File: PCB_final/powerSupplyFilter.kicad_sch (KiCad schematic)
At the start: 3 parts, among them U10 MCP6001T-I_OT

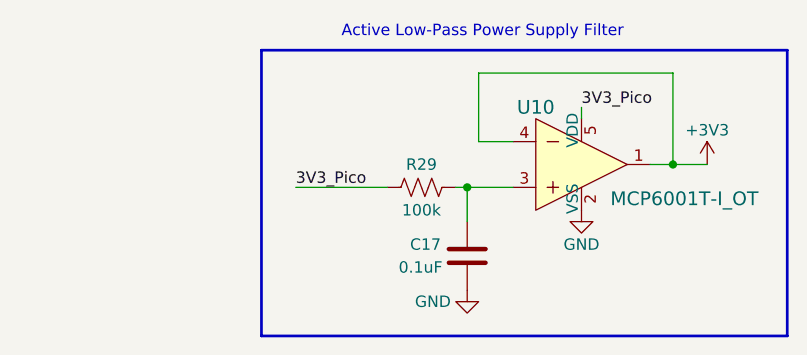
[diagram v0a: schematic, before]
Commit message: Removed filter from schematic and PCB. Adjusted tracings on PCB and schematic for ADC inputs so that each ADC has 14 inputs
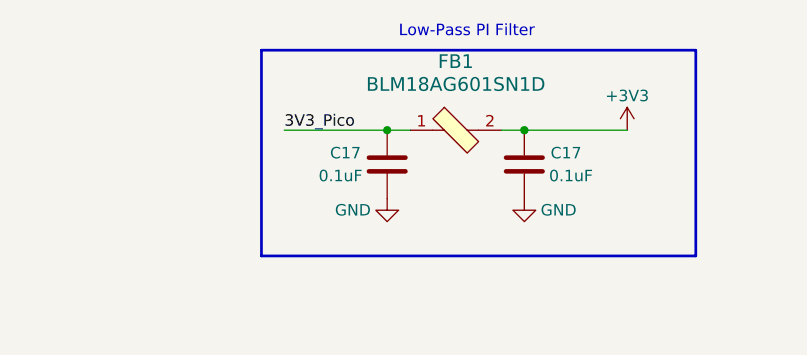
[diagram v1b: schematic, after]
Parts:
- removed R29: 100k, Resistor_SMD:R_0603_1608Metric, symbol Device:R_US
- removed U10: MCP6001T-I_OT, digikey-footprints:SOT-753, symbol dk_Linear-Amplifiers-Instrumentation-OP-Amps-Buffer-Amps:MCP6001T-I_OT
- added C17: 0.1uF, Capacitor_SMD:C_0603_1608Metric, symbol Device:C
- added FB1: BLM18AG601SN1D, digikey-footprints:0603, symbol dk_Ferrite-Beads-and-Chips:BLM18AG601SN1D
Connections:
- net +3V3: now also C17.1, FB1.2
- net 3V3_Pico: now also C17.1, FB1.1
- net GND: now also C17.2
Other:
- note added: "Low-Pass PI Filter"
- note removed: "Active Low-Pass Power Supply Filter"
- moved on the sheet: C17

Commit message: Updated filter's ferrite bead and capacitors on schematic and PCB. Power supply filter now fully integrated
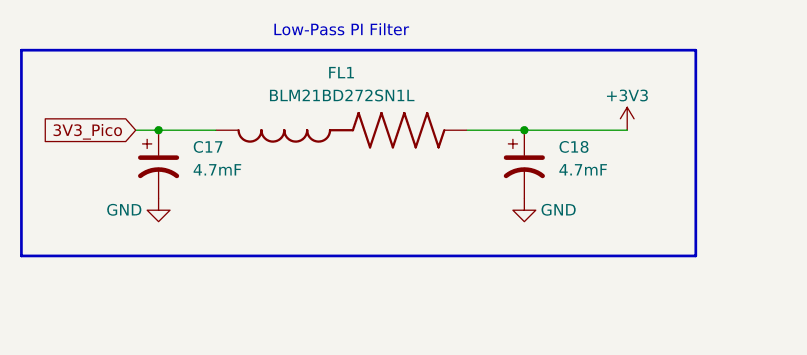
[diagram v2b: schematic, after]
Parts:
- removed C17 (x2): 0.1uF, Capacitor_SMD:C_0603_1608Metric, symbol Device:C
- removed FB1: BLM18AG601SN1D, digikey-footprints:0603, symbol dk_Ferrite-Beads-and-Chips:BLM18AG601SN1D
- added C17, C18: 4.7mF, Capacitor_THT:CP_Radial_D13.0mm_P5.00mm, symbol Device:C_Polarized_US
- added FL1: BLM21BD272SN1L, BEADC2012X145N, symbol BLM21BD272SN1L:BLM21BD272SN1L
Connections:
- net +3V3: now also C18.1, FL1.2
- net 3V3_Pico: now also C17.1, FL1.1
- net GND: now also C17.2, C18.2
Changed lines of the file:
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@@
 (kicad_sch (version 20230121) (generator eeschema)
   (paper "A4")
-  (junction (at 95.25 81.28) (diameter 0) (color 0 0 0 0)
-  )
   (junction (at 110.49 81.28) (diameter 0) (color 0 0 0 0)
   )
-  (wire (pts (xy 107.95 81.28) (xy 110.49 81.28))
-    (stroke (width 0) (type default))
-  )
-  (wire (pts (xy 95.25 81.28) (xy 97.79 81.28))
+  (junction (at 69.85 81.28) (diameter 0) (color 0 0 0 0)
+  )
+  (wire (pts (xy 69.85 81.28) (xy 76.2 81.28))
+    (stroke (width 0) (type default))
+  )
+  (wire (pts (xy 104.14 81.28) (xy 110.49 81.28))
+    (stroke (width 0) (type default))
+  )
+  (wire (pts (xy 67.31 81.28) (xy 69.85 81.28))
     (stroke (width 0) (type default))
   )
@@
     (stroke (width 0) (type default))
   )
-  (wire (pts (xy 83.82 81.28) (xy 95.25 81.28))
-    (stroke (width 0) (type default))
-  )
-  (rectangle (start 81.28 72.39) (end 129.54 95.25)
+  (rectangle (start 54.61 72.39) (end 129.54 95.25)
     (stroke (width 0.3) (type default) (color 0 0 0 1))
     (fill (type none))
   )
-  (text "Low-Pass PI Filter" (at 96.52 71.12 0)
+  (text "Low-Pass PI Filter" (at 82.55 71.12 0)
     (effects (font (size 1.27 1.27)) (justify left bottom))
   )
-  (label "3V3_Pico" (at 83.82 81.28 0) (fields_autoplaced)
-    (effects (font (size 1.27 1.27)) (justify left bottom))
-  )
-  (symbol (lib_id "power:GND") (at 95.25 88.9 0) (unit 1)
+  (global_label "3V3_Pico" (shape input) (at 67.31 81.28 180) (fields_autoplaced)
+    (effects (font (size 1.27 1.27)) (justify right))
+    (property "Intersheetrefs" "${INTERSHEET_REFS}" (at 55.7372 81.28 0)
+      (effects (font (size 1.27 1.27)) (justify right) hide)
+    )
+  )
+  (symbol (lib_id "power:GND") (at 69.85 88.9 0) (unit 1)
     (in_bom yes) (on_board yes) (dnp no)
-    (property "Reference" "#PWR03" (at 95.25 95.25 0)
-      (effects (font (size 1.27 1.27)) hide)
-    )
-    (property "Value" "GND" (at 91.44 90.17 0)
-      (effects (font (size 1.27 1.27)))
-    )
-    (property "Footprint" "" (at 95.25 88.9 0)
-      (effects (font (size 1.27 1.27)) hide)
-    )
-    (property "Datasheet" "" (at 95.25 88.9 0)
+    (property "Reference" "#PWR03" (at 69.85 95.25 0)
+      (effects (font (size 1.27 1.27)) hide)
+    )
+    (property "Value" "GND" (at 66.04 90.17 0)
+      (effects (font (size 1.27 1.27)))
+    )
+    (property "Footprint" "" (at 69.85 88.9 0)
+      (effects (font (size 1.27 1.27)) hide)
+    )
+    (property "Datasheet" "" (at 69.85 88.9 0)
       (effects (font (size 1.27 1.27)) hide)
     )
@@
     )
   )
-  (symbol (lib_id "Device:C") (at 110.49 85.09 0) (mirror y) (unit 1)
-    (in_bom yes) (on_board yes) (dnp no)
-    (property "Reference" "C17" (at 116.84 83.82 0)
-      (effects (font (size 1.27 1.27)) (justify left))
-    )
-    (property "Value" "0.1uF" (at 118.11 86.36 0)
-      (effects (font (size 1.27 1.27)) (justify left))
-    )
-    (property "Footprint" "Capacitor_SMD:C_0603_1608Metric" (at 109.5248 88.9 0)
-      (effects (font (size 1.27 1.27)) hide)
-    )
-    (property "Datasheet" "~" (at 110.49 85.09 0)
-      (effects (font (size 1.27 1.27)) hide)
+  (symbol (lib_id "BLM21BD272SN1L:BLM21BD272SN1L") (at 91.44 81.28 0) (unit 1)
+    (in_bom yes) (on_board yes) (dnp no) (fields_autoplaced)
+    (property "Reference" "FL1" (at 90.17 74.93 0)
+      (effects (font (size 1.27 1.27)))
+    )
+    (property "Value" "BLM21BD272SN1L" (at 90.17 77.47 0)
+      (effects (font (size 1.27 1.27)))
+    )
+    (property "Footprint" "BEADC2012X145N" (at 91.44 81.28 0)
+      (effects (font (size 1.27 1.27)) (justify left bottom) hide)
+    )
+    (property "Datasheet" "" (at 91.44 81.28 0)
+      (effects (font (size 1.27 1.27)) (justify left bottom) hide)
     )
     (pin "1")
     (pin "2")
     (instances
-      (project "interface_board"
-        (path "/2096cfcb-1c5f-4ebc-ae85-e59f8ec52ec3"
-          (reference "C17") (unit 1)
-        )
-      )
-      (project "PCB_final"
-        (path "/e4192969-4b4c-4bbf-a0a8-ef09d84e64d7"
-          (reference "C2") (unit 1)
-        )
-        (path "/e4192969-4b4c-4bbf-a0a8-ef09d84e64d7/e0559890-1aa0-4336-9a3e-110d23fe279d"
-          (reference "C17") (unit 1)
-        )
+      (project "PCB_final"
+        (path "/e4192969-4b4c-4bbf-a0a8-ef09d84e64d7/4a059b75-7de0-4eb9-8588-5d4fb226c6d3"
+          (reference "FL1") (unit 1)
+        )
+      )
+    )
+  )
+  (symbol (lib_id "Device:C_Polarized_US") (at 110.49 85.09 0) (unit 1)
+    (in_bom yes) (on_board yes) (dnp no) (fields_autoplaced)
+    (property "Reference" "C18" (at 114.3 83.185 0)
+      (effects (font (size 1.27 1.27)) (justify left))
+    )
+    (property "Value" "4.7mF" (at 114.3 85.725 0)
+      (effects (font (size 1.27 1.27)) (justify left))
+    )
+    (property "Footprint" "Capacitor_THT:CP_Radial_D13.0mm_P5.00mm" (at 110.49 85.09 0)
+      (effects (font (size 1.27 1.27)) hide)
+    )
+    (property "Datasheet" "https://connect.kemet.com:7667/gateway/IntelliData-ComponentDocumentation/1.0/download/datasheet/ESK478M6R3AL3AA" (at 110.49 85.09 0)
+      (effects (font (size 1.27 1.27)) hide)
+    )
+    (property "Evan Desmond" "" (at 110.49 85.09 0)
+      (effects (font (size 1.27 1.27)) hide)
+    )
+    (pin "1")
+    (pin "2")
+    (instances
+      (project "PCB_final"
         (path "/e4192969-4b4c-4bbf-a0a8-ef09d84e64d7/4a059b75-7de0-4eb9-8588-5d4fb226c6d3"
           (reference "C18") (unit 1)
-        )
-      )
-    )
-  )
-  (symbol (lib_id "Device:C") (at 95.25 85.09 0) (unit 1)
-    (in_bom yes) (on_board yes) (dnp no)
-    (property "Reference" "C17" (at 88.9 83.82 0)
-      (effects (font (size 1.27 1.27)) (justify left))
-    )
-    (property "Value" "0.1uF" (at 87.63 86.36 0)
-      (effects (font (size 1.27 1.27)) (justify left))
-    )
-    (property "Footprint" "Capacitor_SMD:C_0603_1608Metric" (at 96.2152 88.9 0)
-      (effects (font (size 1.27 1.27)) hide)
-    )
-    (property "Datasheet" "~" (at 95.25 85.09 0)
-      (effects (font (size 1.27 1.27)) hide)
-    )
-    (pin "1")
-    (pin "2")
-    (instances
-      (project "interface_board"
-        (path "/2096cfcb-1c5f-4ebc-ae85-e59f8ec52ec3"
-          (reference "C17") (unit 1)
-        )
-      )
-      (project "PCB_final"
-        (path "/e4192969-4b4c-4bbf-a0a8-ef09d84e64d7"
-          (reference "C2") (unit 1)
-        )
-        (path "/e4192969-4b4c-4bbf-a0a8-ef09d84e64d7/e0559890-1aa0-4336-9a3e-110d23fe279d"
-          (reference "C17") (unit 1)
-        )
-        (path "/e4192969-4b4c-4bbf-a0a8-ef09d84e64d7/4a059b75-7de0-4eb9-8588-5d4fb226c6d3"
-          (reference "C17") (unit 1)
         )
       )
@@
     )
   )
-  (symbol (lib_id "dk_Ferrite-Beads-and-Chips:BLM18AG601SN1D") (at 102.87 81.28 0) (unit 1)
+  (symbol (lib_id "Device:C_Polarized_US") (at 69.85 85.09 0) (unit 1)
     (in_bom yes) (on_board yes) (dnp no) (fields_autoplaced)
-    (property "Reference" "FB1" (at 102.87 73.66 0)
-      (effects (font (size 1.524 1.524)))
-    )
-    (property "Value" "BLM18AG601SN1D" (at 102.87 76.2 0)
-      (effects (font (size 1.524 1.524)))
-    )
-    (property "Footprint" "digikey-footprints:0603" (at 107.95 76.2 0)
-      (effects (font (size 1.524 1.524)) (justify left) hide)
-    )
-    (property "Datasheet" "https://www.murata.com/en-us/products/productdata/8796738650142/ENFA0003.pdf" (at 107.95 73.66 0)
-      (effects (font (size 1.524 1.524)) (justify left) hide)
-    )
-    (property "Digi-Key_PN" "490-1014-1-ND" (at 107.95 71.12 0)
-      (effects (font (size 1.524 1.524)) (justify left) hide)
-    )
-    (property "MPN" "BLM18AG601SN1D" (at 107.95 68.58 0)
-      (effects (font (size 1.524 1.524)) (justify left) hide)
-    )
-    (property "Category" "Filters" (at 107.95 66.04 0)
-      (effects (font (size 1.524 1.524)) (justify left) hide)
-    )
-    (property "Family" "Ferrite Beads and Chips" (at 107.95 63.5 0)
-      (effects (font (size 1.524 1.524)) (justify left) hide)
-    )
-    (property "DK_Datasheet_Link" "https://www.murata.com/en-us/products/productdata/8796738650142/ENFA0003.pdf" (at 107.95 60.96 0)
-      (effects (font (size 1.524 1.524)) (justify left) hide)
-    )
-    (property "DK_Detail_Page" "/product-detail/en/murata-electronics-north-america/BLM18AG601SN1D/490-1014-1-ND/584462" (at 107.95 58.42 0)
-      (effects (font (size 1.524 1.524)) (justify left) hide)
-    )
-    (property "Description" "FERRITE BEAD 600 OHM 0603 1LN" (at 107.95 55.88 0)
-      (effects (font (size 1.524 1.524)) (justify left) hide)
-    )
-    (property "Manufacturer" "Murata Electronics North America" (at 107.95 53.34 0)
-      (effects (font (size 1.524 1.524)) (justify left) hide)
-    )
-    (property "Status" "Active" (at 107.95 50.8 0)
-      (effects (font (size 1.524 1.524)) (justify left) hide)
-    )
-    (property "Evan Desmond" "" (at 102.87 81.28 0)
+    (property "Reference" "C17" (at 73.66 83.185 0)
+      (effects (font (size 1.27 1.27)) (justify left))
+    )
+    (property "Value" "4.7mF" (at 73.66 85.725 0)
+      (effects (font (size 1.27 1.27)) (justify left))
+    )
+    (property "Footprint" "Capacitor_THT:CP_Radial_D13.0mm_P5.00mm" (at 69.85 85.09 0)
+      (effects (font (size 1.27 1.27)) hide)
+    )
+    (property "Datasheet" "https://connect.kemet.com:7667/gateway/IntelliData-ComponentDocumentation/1.0/download/datasheet/ESK478M6R3AL3AA" (at 69.85 85.09 0)
+      (effects (font (size 1.27 1.27)) hide)
+    )
+    (property "Evan Desmond" "" (at 69.85 85.09 0)
       (effects (font (size 1.27 1.27)) hide)
     )
@@
       (project "PCB_final"
         (path "/e4192969-4b4c-4bbf-a0a8-ef09d84e64d7/4a059b75-7de0-4eb9-8588-5d4fb226c6d3"
-          (reference "FB1") (unit 1)
-        )
-      )
+          (reference "C17") (unit 1)
+        )
+      )

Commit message: Added 2 bypass capacitors for VREF pins on ADCs on schematic. Placed caps on PCB and rerouted traces to pass DRC. Increased trace thickness for 3v3 on ADCs to 0.35mm and 0.75mm going from PICO 3v3 to power supply filter to 3v3. Also re-arranged silkscreen to be visible when ribbon cable connectors are installed. Moved mounting holes to be accesible once ribbon cables are installed
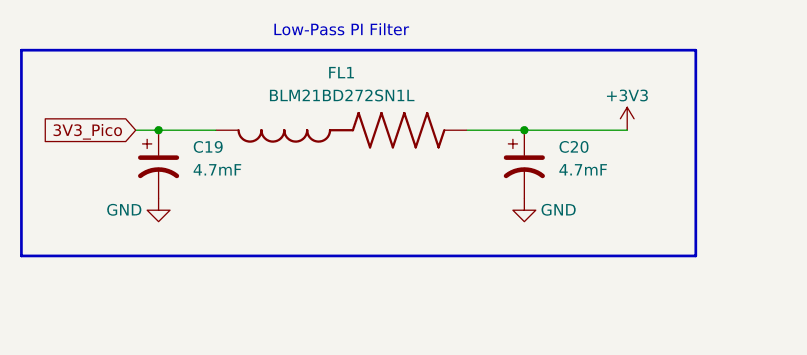
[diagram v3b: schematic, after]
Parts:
- renumbered C17 to C19, C18 to C20
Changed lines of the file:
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@@
   (symbol (lib_id "Device:C_Polarized_US") (at 110.49 85.09 0) (unit 1)
     (in_bom yes) (on_board yes) (dnp no) (fields_autoplaced)
-    (property "Reference" "C18" (at 114.3 83.185 0)
+    (property "Reference" "C20" (at 114.3 83.185 0)
       (effects (font (size 1.27 1.27)) (justify left))
     )
@@
       (project "PCB_final"
         (path "/e4192969-4b4c-4bbf-a0a8-ef09d84e64d7/4a059b75-7de0-4eb9-8588-5d4fb226c6d3"
-          (reference "C18") (unit 1)
+          (reference "C20") (unit 1)
         )
       )
@@
   (symbol (lib_id "Device:C_Polarized_US") (at 69.85 85.09 0) (unit 1)
     (in_bom yes) (on_board yes) (dnp no) (fields_autoplaced)
-    (property "Reference" "C17" (at 73.66 83.185 0)
+    (property "Reference" "C19" (at 73.66 83.185 0)
       (effects (font (size 1.27 1.27)) (justify left))
     )
@@
       (project "PCB_final"
         (path "/e4192969-4b4c-4bbf-a0a8-ef09d84e64d7/4a059b75-7de0-4eb9-8588-5d4fb226c6d3"
-          (reference "C17") (unit 1)
+          (reference "C19") (unit 1)
         )
       )

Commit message: Updated kicad PCB to use both SPI channels of the RPI Pico
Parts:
- FL1: footprint BEADC2012X145N -> capstone_custom:BEADC2012X145N
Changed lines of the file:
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@@
       (effects (font (size 1.27 1.27)))
     )
-    (property "Footprint" "BEADC2012X145N" (at 91.44 81.28 0)
+    (property "Footprint" "capstone_custom:BEADC2012X145N" (at 91.44 81.28 0)
       (effects (font (size 1.27 1.27)) (justify left bottom) hide)
     )

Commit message: Updated titles and revision dates on schematics
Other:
- company: (none) -> https://github.com/yoctometric/pressure-mat
- title: (none) -> ECE406 Pressure Mat Interface PCB
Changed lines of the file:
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@@
 (kicad_sch (version 20230121) (generator eeschema)
   (paper "A4")
+  (title_block
+    (title "ECE406 Pressure Mat Interface PCB")
+    (date "2023-12-05")
+    (rev "1.1")
+    (company "https://github.com/yoctometric/pressure-mat")
+  )
   (junction (at 110.49 81.28) (diameter 0) (color 0 0 0 0)
   )
